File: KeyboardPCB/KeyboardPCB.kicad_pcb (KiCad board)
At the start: 2 copper layers, 182 parts, among them P1 USB_C_Plug, P2 USB_C_Plug, Q1 CSD17527Q5A, Q2 CSD17527Q5A, U1 ATmega32U4-M, U2 TPS61236PRWLT, U3 BQ297xy, U4 BQ24193RGER, Y1 ECS-160-7-33B-CKL-TR

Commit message: Began work on PCB
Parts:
- moved D7 160.3 mm to (25.4, 157.5), turned to 90 degrees
- moved Y1 156.5 mm to (36.7, 34.0)
- moved D6 147.1 mm to (25.4, 134.6), turned to 90 degrees
- moved D12 144.0 mm to (36.3, 157.5), turned to 90 degrees
- moved D5 135.8 mm to (25.4, 111.8), turned to 90 degrees
- moved D16 135.3 mm to (50.5, 136.5), turned to 90 degrees
- moved R3 132.4 mm to (35.6, 27.9)
- moved D11 127.8 mm to (38.1, 131.4), turned to 90 degrees
- moved D4 127.6 mm to (25.4, 90.7), turned to 90 degrees
- moved C2 124.8 mm to (44.0, 35.6)
- moved C1 124.7 mm to (44.0, 33.0)
- moved D3 121.9 mm to (25.4, 71.1), turned to 90 degrees
- moved D15 120.2 mm to (53.0, 114.3), turned to 90 degrees
- moved C9 119.3 mm to (55.9, 22.9), turned to -90 degrees
- moved D20 119.2 mm to (63.5, 136.5), turned to 90 degrees
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
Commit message: Changed switch and revised PCB layout?
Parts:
- BT1, C1, C11, C2, C3, C4, C5, C6, C7, C8, C9, L1, L2, LED1, LED2, LED3, LED4, LED5, P1, P2, Q1, Q2, R1, R10, R11, R12, R13, R14, R15, R16, R2, R3, R4, R5, R6, R7, R8, R9, S1, U1, U2, U3, U4, Y1: moved to B.Cu
- S10, S11, S12, S13, S14, S15, S16, S17, S18, S19, S2, S20, S21, S22, S23, S24, S25, S26, S27, S28, S29, S3, S30, S31, S32, S33, S34, S35, S36, S37, S38, S39, S4, S40, S41, S42, S43, S44, S45, S46, S47, S48, S49, S5, S50, S51, S52, S53, S54, S55, S56, S57, S58, S59, S6, S60, S61, S62, S63, S64, S65, S66, S67, S68, S69, S7, S70, S8, S9: footprint keyboard_syms:B3FS1012P -> keyboard_syms:B3U1100PB
- moved D7 249.8 mm to (245.0, 38.4), turned to 0 degrees
- moved D6 240.7 mm to (245.0, 36.0), turned to 0 degrees
- moved D12 234.4 mm to (245.0, 50.7), turned to 0 degrees
- moved D5 233.1 mm to (245.0, 33.5), turned to 0 degrees
- moved D4 227.5 mm to (245.0, 31.1), turned to 0 degrees
- moved D16 224.3 mm to (248.6, 31.1), turned to 0 degrees
- moved D3 223.6 mm to (245.0, 28.6), turned to 0 degrees
- moved D11 223.0 mm to (245.0, 48.2), turned to 0 degrees
- moved D10 216.7 mm to (245.0, 45.8), turned to 0 degrees
- moved D15 213.5 mm to (248.6, 28.6), turned to 0 degrees
- moved D9 212.7 mm to (245.0, 43.3), turned to 0 degrees
- moved D8 211.9 mm to (245.0, 40.9), turned to 0 degrees
- moved D20 208.3 mm to (248.6, 40.9), turned to 0 degrees
- moved U1 201.6 mm to (207.3, 122.4), turned to 180 degrees
- moved D19 199.7 mm to (248.6, 38.4), turned to 0 degrees
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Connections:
- D22 pad 2: Net-(D22-A) -> unconnected-(D22-A-Pad2)
- D25 pad 2: Net-(D25-A) -> unconnected-(D25-A-Pad2)
- D29 pad 2: Net-(D29-A) -> unconnected-(D29-A-Pad2)
- D38 pad 2: Net-(D38-A) -> unconnected-(D38-A-Pad2)
- D39 pad 2: Net-(D39-A) -> unconnected-(D39-A-Pad2)
- S10 pad 1: unconnected-(S10-C1-Pad1) -> /Key_Array/ICOL1
- S10 pad 2: /Key_Array/ICOL1 -> Net-(D11-A)
- S10 pad 3: Net-(D11-A) -> unconnected-(S10-NC-Pad3)
- S11 pad 1: unconnected-(S11-C1-Pad1) -> /Key_Array/ICOL1
- S11 pad 2: /Key_Array/ICOL1 -> Net-(D12-A)
- S11 pad 3: Net-(D12-A) -> unconnected-(S11-NC-Pad3)
- S12 pad 1: unconnected-(S12-C1-Pad1) -> /Key_Array/ICOL2
- S12 pad 2: /Key_Array/ICOL2 -> Net-(D13-A)
- S12 pad 3: Net-(D13-A) -> unconnected-(S12-NC-Pad3)
- S13 pad 1: unconnected-(S13-C1-Pad1) -> /Key_Array/ICOL2
- S13 pad 2: /Key_Array/ICOL2 -> Net-(D14-A)
- S13 pad 3: Net-(D14-A) -> unconnected-(S13-NC-Pad3)
- S14 pad 1: unconnected-(S14-C1-Pad1) -> /Key_Array/ICOL2
- S14 pad 2: /Key_Array/ICOL2 -> Net-(D15-A)
- S14 pad 3: Net-(D15-A) -> unconnected-(S14-NC-Pad3)
- S15 pad 1: unconnected-(S15-C1-Pad1) -> /Key_Array/ICOL2
- S15 pad 2: /Key_Array/ICOL2 -> Net-(D16-A)
- S15 pad 3: Net-(D16-A) -> unconnected-(S15-NC-Pad3)
- S16 pad 1: unconnected-(S16-C1-Pad1) -> /Key_Array/ICOL3
- S16 pad 2: /Key_Array/ICOL3 -> Net-(D17-A)
- S16 pad 3: Net-(D17-A) -> unconnected-(S16-NC-Pad3)
- S17 pad 1: unconnected-(S17-C1-Pad1) -> /Key_Array/ICOL3
- S17 pad 2: /Key_Array/ICOL3 -> Net-(D18-A)
- S17 pad 3: Net-(D18-A) -> unconnected-(S17-NC-Pad3)
- S18 pad 1: unconnected-(S18-C1-Pad1) -> /Key_Array/ICOL3
- S18 pad 2: /Key_Array/ICOL3 -> Net-(D19-A)
- S18 pad 3: Net-(D19-A) -> unconnected-(S18-NC-Pad3)
- S19 pad 1: unconnected-(S19-C1-Pad1) -> /Key_Array/ICOL3
- S19 pad 2: /Key_Array/ICOL3 -> Net-(D20-A)
- S19 pad 3: Net-(D20-A) -> unconnected-(S19-NC-Pad3)
- S2 pad 1: unconnected-(S2-C1-Pad1) -> /Key_Array/ICOL0
- S2 pad 2: /Key_Array/ICOL0 -> Net-(D3-A)
- S2 pad 3: Net-(D3-A) -> unconnected-(S2-NC-Pad3)
- S20 pad 1: unconnected-(S20-C1-Pad1) -> /Key_Array/ICOL4
- S20 pad 2: /Key_Array/ICOL4 -> Net-(D21-A)
- S20 pad 3: Net-(D21-A) -> unconnected-(S20-NC-Pad3)
- S21 pad 1: unconnected-(S21-C1-Pad1) -> /Key_Array/ICOL4
- S21 pad 2: /Key_Array/ICOL4 -> unconnected-(S21-C2-Pad2)
- S21 pad 3: Net-(D22-A) -> unconnected-(S21-NC-Pad3)
- S22 pad 1: unconnected-(S22-C1-Pad1) -> /Key_Array/ICOL4
- S22 pad 2: /Key_Array/ICOL4 -> Net-(D23-A)
- S22 pad 3: Net-(D23-A) -> unconnected-(S22-NC-Pad3)
- S23 pad 1: unconnected-(S23-C1-Pad1) -> /Key_Array/ICOL4
- S23 pad 2: /Key_Array/ICOL4 -> Net-(D24-A)
- S23 pad 3: Net-(D24-A) -> unconnected-(S23-NC-Pad3)
- S24 pad 2: /Key_Array/ICOL5 -> unconnected-(S24-C2-Pad2)
- S24 pad 3: Net-(D25-A) -> unconnected-(S24-NC-Pad3)
- S25 pad 1: unconnected-(S25-C1-Pad1) -> /Key_Array/ICOL5
- S25 pad 2: /Key_Array/ICOL5 -> Net-(D26-A)
- S25 pad 3: Net-(D26-A) -> unconnected-(S25-NC-Pad3)
- S26 pad 1: unconnected-(S26-C1-Pad1) -> /Key_Array/ICOL5
- S26 pad 2: /Key_Array/ICOL5 -> Net-(D27-A)
- S26 pad 3: Net-(D27-A) -> unconnected-(S26-NC-Pad3)
- S27 pad 1: unconnected-(S27-C1-Pad1) -> /Key_Array/ICOL5
- S27 pad 2: /Key_Array/ICOL5 -> Net-(D28-A)
- S27 pad 3: Net-(D28-A) -> unconnected-(S27-NC-Pad3)
- S28 pad 2: /Key_Array/ICOL6 -> unconnected-(S28-C2-Pad2)
- S28 pad 3: Net-(D29-A) -> unconnected-(S28-NC-Pad3)
- S29 pad 1: unconnected-(S29-C1-Pad1) -> /Key_Array/ICOL6
- S29 pad 2: /Key_Array/ICOL6 -> Net-(D30-A)
- S29 pad 3: Net-(D30-A) -> unconnected-(S29-NC-Pad3)
- S3 pad 1: unconnected-(S3-C1-Pad1) -> /Key_Array/ICOL0
- S3 pad 2: /Key_Array/ICOL0 -> Net-(D4-A)
- S3 pad 3: Net-(D4-A) -> unconnected-(S3-NC-Pad3)
- S30 pad 1: unconnected-(S30-C1-Pad1) -> /Key_Array/ICOL6
- S30 pad 2: /Key_Array/ICOL6 -> Net-(D31-A)
- S30 pad 3: Net-(D31-A) -> unconnected-(S30-NC-Pad3)
- S31 pad 1: unconnected-(S31-C1-Pad1) -> /Key_Array/ICOL6
- S31 pad 2: /Key_Array/ICOL6 -> Net-(D32-A)
- S31 pad 3: Net-(D32-A) -> unconnected-(S31-NC-Pad3)
- S32 pad 1: unconnected-(S32-C1-Pad1) -> /Key_Array/ICOL6
- S32 pad 2: /Key_Array/ICOL6 -> Net-(D33-A)
- S32 pad 3: Net-(D33-A) -> unconnected-(S32-NC-Pad3)
- S33 pad 1: unconnected-(S33-C1-Pad1) -> /Key_Array/ICOL7
- S33 pad 2: /Key_Array/ICOL7 -> Net-(D34-A)
- S33 pad 3: Net-(D34-A) -> unconnected-(S33-NC-Pad3)
- S34 pad 1: unconnected-(S34-C1-Pad1) -> /Key_Array/ICOL7
- S34 pad 2: /Key_Array/ICOL7 -> Net-(D35-A)
- S34 pad 3: Net-(D35-A) -> unconnected-(S34-NC-Pad3)
- S35 pad 1: unconnected-(S35-C1-Pad1) -> /Key_Array/ICOL7
- S35 pad 2: /Key_Array/ICOL7 -> Net-(D36-A)
- S35 pad 3: Net-(D36-A) -> unconnected-(S35-NC-Pad3)
- S36 pad 1: unconnected-(S36-C1-Pad1) -> /Key_Array/ICOL7
- S36 pad 2: /Key_Array/ICOL7 -> Net-(D37-A)
- S36 pad 3: Net-(D37-A) -> unconnected-(S36-NC-Pad3)
- S37 pad 1: unconnected-(S37-C1-Pad1) -> /Key_Array/ICOL7
- S37 pad 2: /Key_Array/ICOL7 -> unconnected-(S37-C2-Pad2)
- S37 pad 3: Net-(D38-A) -> unconnected-(S37-NC-Pad3)
- S38 pad 2: /Key_Array/ICOL8 -> unconnected-(S38-C2-Pad2)
- S38 pad 3: Net-(D39-A) -> unconnected-(S38-NC-Pad3)
- S39 pad 1: unconnected-(S39-C1-Pad1) -> /Key_Array/ICOL8
- S39 pad 2: /Key_Array/ICOL8 -> Net-(D40-A)
- S39 pad 3: Net-(D40-A) -> unconnected-(S39-NC-Pad3)
- S4 pad 1: unconnected-(S4-C1-Pad1) -> /Key_Array/ICOL0
- S4 pad 2: /Key_Array/ICOL0 -> Net-(D5-A)
- S4 pad 3: Net-(D5-A) -> unconnected-(S4-NC-Pad3)
- S40 pad 1: unconnected-(S40-C1-Pad1) -> /Key_Array/ICOL8
- S40 pad 2: /Key_Array/ICOL8 -> Net-(D41-A)
- S40 pad 3: Net-(D41-A) -> unconnected-(S40-NC-Pad3)
- S41 pad 1: unconnected-(S41-C1-Pad1) -> /Key_Array/ICOL8
- S41 pad 2: /Key_Array/ICOL8 -> Net-(D42-A)
- S41 pad 3: Net-(D42-A) -> unconnected-(S41-NC-Pad3)
- S42 pad 1: unconnected-(S42-C1-Pad1) -> /Key_Array/ICOL9
- S42 pad 2: /Key_Array/ICOL9 -> Net-(D43-A)
- S42 pad 3: Net-(D43-A) -> unconnected-(S42-NC-Pad3)
- S43 pad 1: unconnected-(S43-C1-Pad1) -> /Key_Array/ICOL9
- S43 pad 2: /Key_Array/ICOL9 -> Net-(D44-A)
- S43 pad 3: Net-(D44-A) -> unconnected-(S43-NC-Pad3)
- S44 pad 1: unconnected-(S44-C1-Pad1) -> /Key_Array/ICOL9
- S44 pad 2: /Key_Array/ICOL9 -> Net-(D45-A)
- S44 pad 3: Net-(D45-A) -> unconnected-(S44-NC-Pad3)
- S45 pad 1: unconnected-(S45-C1-Pad1) -> /Key_Array/ICOL9
- S45 pad 2: /Key_Array/ICOL9 -> Net-(D46-A)
- S45 pad 3: Net-(D46-A) -> unconnected-(S45-NC-Pad3)
- S46 pad 1: unconnected-(S46-C1-Pad1) -> /Key_Array/ICOL10
- S46 pad 2: /Key_Array/ICOL10 -> Net-(D47-A)
- S46 pad 3: Net-(D47-A) -> unconnected-(S46-NC-Pad3)
- S47 pad 1: unconnected-(S47-C1-Pad1) -> /Key_Array/ICOL10
- S47 pad 2: /Key_Array/ICOL10 -> Net-(D48-A)
- S47 pad 3: Net-(D48-A) -> unconnected-(S47-NC-Pad3)
- S48 pad 1: unconnected-(S48-C1-Pad1) -> /Key_Array/ICOL10
- S48 pad 2: /Key_Array/ICOL10 -> Net-(D49-A)
- S48 pad 3: Net-(D49-A) -> unconnected-(S48-NC-Pad3)
- S49 pad 1: unconnected-(S49-C1-Pad1) -> /Key_Array/ICOL10
- S49 pad 2: /Key_Array/ICOL10 -> Net-(D50-A)
- S49 pad 3: Net-(D50-A) -> unconnected-(S49-NC-Pad3)
- S5 pad 1: unconnected-(S5-C1-Pad1) -> /Key_Array/ICOL0
- S5 pad 2: /Key_Array/ICOL0 -> Net-(D6-A)
- S5 pad 3: Net-(D6-A) -> unconnected-(S5-NC-Pad3)
- S50 pad 1: unconnected-(S50-C1-Pad1) -> /Key_Array/ICOL11
- S50 pad 2: /Key_Array/ICOL11 -> Net-(D51-A)
- S50 pad 3: Net-(D51-A) -> unconnected-(S50-NC-Pad3)
- S51 pad 1: unconnected-(S51-C1-Pad1) -> /Key_Array/ICOL11
- S51 pad 2: /Key_Array/ICOL11 -> Net-(D52-A)
- S51 pad 3: Net-(D52-A) -> unconnected-(S51-NC-Pad3)
- S52 pad 1: unconnected-(S52-C1-Pad1) -> /Key_Array/ICOL11
- S52 pad 2: /Key_Array/ICOL11 -> Net-(D53-A)
- S52 pad 3: Net-(D53-A) -> unconnected-(S52-NC-Pad3)
- S53 pad 1: unconnected-(S53-C1-Pad1) -> /Key_Array/ICOL11
- S53 pad 2: /Key_Array/ICOL11 -> Net-(D54-A)
- S53 pad 3: Net-(D54-A) -> unconnected-(S53-NC-Pad3)
- S54 pad 1: unconnected-(S54-C1-Pad1) -> /Key_Array/ICOL11
- S54 pad 2: /Key_Array/ICOL11 -> Net-(D55-A)
- S54 pad 3: Net-(D55-A) -> unconnected-(S54-NC-Pad3)
- S55 pad 1: unconnected-(S55-C1-Pad1) -> /Key_Array/ICOL12
- S55 pad 2: /Key_Array/ICOL12 -> Net-(D56-A)
- S55 pad 3: Net-(D56-A) -> unconnected-(S55-NC-Pad3)
- S56 pad 1: unconnected-(S56-C1-Pad1) -> /Key_Array/ICOL12
- S56 pad 2: /Key_Array/ICOL12 -> Net-(D57-A)
- S56 pad 3: Net-(D57-A) -> unconnected-(S56-NC-Pad3)
- S57 pad 1: unconnected-(S57-C1-Pad1) -> /Key_Array/ICOL12
- S57 pad 2: /Key_Array/ICOL12 -> Net-(D58-A)
- S57 pad 3: Net-(D58-A) -> unconnected-(S57-NC-Pad3)
- S58 pad 1: unconnected-(S58-C1-Pad1) -> /Key_Array/ICOL12
- S58 pad 2: /Key_Array/ICOL12 -> Net-(D59-A)
- S58 pad 3: Net-(D59-A) -> unconnected-(S58-NC-Pad3)
- S59 pad 1: unconnected-(S59-C1-Pad1) -> /Key_Array/ICOL12
- S59 pad 2: /Key_Array/ICOL12 -> Net-(D60-A)
- S59 pad 3: Net-(D60-A) -> unconnected-(S59-NC-Pad3)
- S6 pad 1: unconnected-(S6-C1-Pad1) -> /Key_Array/ICOL0
- S6 pad 2: /Key_Array/ICOL0 -> Net-(D7-A)
- S6 pad 3: Net-(D7-A) -> unconnected-(S6-NC-Pad3)
- S60 pad 1: unconnected-(S60-C1-Pad1) -> /Key_Array/ICOL13
- S60 pad 2: /Key_Array/ICOL13 -> Net-(D61-A)
- S60 pad 3: Net-(D61-A) -> unconnected-(S60-NC-Pad3)
- S61 pad 1: unconnected-(S61-C1-Pad1) -> /Key_Array/ICOL13
- S61 pad 2: /Key_Array/ICOL13 -> Net-(D62-A)
- S61 pad 3: Net-(D62-A) -> unconnected-(S61-NC-Pad3)
- S62 pad 1: unconnected-(S62-C1-Pad1) -> /Key_Array/ICOL13
- S62 pad 2: /Key_Array/ICOL13 -> Net-(D63-A)
- S62 pad 3: Net-(D63-A) -> unconnected-(S62-NC-Pad3)
- S63 pad 1: unconnected-(S63-C1-Pad1) -> /Key_Array/ICOL13
- S63 pad 2: /Key_Array/ICOL13 -> Net-(D64-A)
- S63 pad 3: Net-(D64-A) -> unconnected-(S63-NC-Pad3)
- S64 pad 1: unconnected-(S64-C1-Pad1) -> /Key_Array/ICOL13
- S64 pad 2: /Key_Array/ICOL13 -> Net-(D65-A)
- S64 pad 3: Net-(D65-A) -> unconnected-(S64-NC-Pad3)
- S65 pad 1: unconnected-(S65-C1-Pad1) -> /Key_Array/ICOL14
- S65 pad 2: /Key_Array/ICOL14 -> Net-(D66-A)
- S65 pad 3: Net-(D66-A) -> unconnected-(S65-NC-Pad3)
- S66 pad 1: unconnected-(S66-C1-Pad1) -> /Key_Array/ICOL14
- S66 pad 2: /Key_Array/ICOL14 -> Net-(D67-A)
- S66 pad 3: Net-(D67-A) -> unconnected-(S66-NC-Pad3)
- S67 pad 1: unconnected-(S67-C1-Pad1) -> /Key_Array/ICOL14
- S67 pad 2: /Key_Array/ICOL14 -> Net-(D68-A)
- S67 pad 3: Net-(D68-A) -> unconnected-(S67-NC-Pad3)
- S68 pad 1: unconnected-(S68-C1-Pad1) -> /Key_Array/ICOL15
- S68 pad 2: /Key_Array/ICOL15 -> Net-(D69-A)
- S68 pad 3: Net-(D69-A) -> unconnected-(S68-NC-Pad3)
- S69 pad 1: unconnected-(S69-C1-Pad1) -> /Key_Array/ICOL15
- S69 pad 2: /Key_Array/ICOL15 -> Net-(D70-A)
- S69 pad 3: Net-(D70-A) -> unconnected-(S69-NC-Pad3)
- S7 pad 1: unconnected-(S7-C1-Pad1) -> /Key_Array/ICOL1
- S7 pad 2: /Key_Array/ICOL1 -> Net-(D8-A)
- S7 pad 3: Net-(D8-A) -> unconnected-(S7-NC-Pad3)
- S70 pad 1: unconnected-(S70-C1-Pad1) -> /Key_Array/ICOL15
- S70 pad 2: /Key_Array/ICOL15 -> Net-(D71-A)
- S70 pad 3: Net-(D71-A) -> unconnected-(S70-NC-Pad3)
- S8 pad 1: unconnected-(S8-C1-Pad1) -> /Key_Array/ICOL1
- S8 pad 2: /Key_Array/ICOL1 -> Net-(D9-A)
- S8 pad 3: Net-(D9-A) -> unconnected-(S8-NC-Pad3)
- S9 pad 1: unconnected-(S9-C1-Pad1) -> /Key_Array/ICOL1
- S9 pad 2: /Key_Array/ICOL1 -> Net-(D10-A)
- S9 pad 3: Net-(D10-A) -> unconnected-(S9-NC-Pad3)
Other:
- board outline added: 81.3 x 50.8 mm
- board text added: "1"
- board text added: "Esc"
- board text added: "Q1"

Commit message: Finalised schematic, progress on board layout
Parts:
- removed C11: UMK107ABJ105KA8T, keyboard_syms:CAPC1608X95N
- removed D68, D69, D70, D71: 1N4148WT, Diode_SMD:D_SOD-523
- removed S69: MX_PGDN1, keyboard_syms:B3U1100PB
- removed S70: MX_FN1, keyboard_syms:B3U1100PB
- added C10: UMK107ABJ105KA8T, keyboard_syms:CAPC1608X95N, B.Cu at (210.9, 126.2)
- added D1: 1N4148WT, Diode_SMD:D_SOD-523, F.Cu at (63.5, 47.0)
- added D2: 1N4148WT, Diode_SMD:D_SOD-523, F.Cu at (63.5, 58.4)
- C1: value GRM21BC81C226ME44L -> UMK107ABJ105KA8T; footprint keyboard_syms:CAPC2012X145N -> keyboard_syms:CAPC1608X95N
- C3, C5: value UMK107ABJ105KA8T -> GRM21BC81C226ME44L; footprint keyboard_syms:CAPC1608X95N -> keyboard_syms:CAPC2012X145N
- C4: value C0603C104K1RACAUTO -> UMK107ABJ105KA8T
- C6: value MSASJ021SB5472KWNA01 -> GRM21BC81C226ME44L; footprint keyboard_syms:CAPC0201X14N -> keyboard_syms:CAPC2012X145N
- C8: value GRM21BC81C226ME44L -> MSASJ021SB5472KWNA01; footprint keyboard_syms:CAPC2012X145N -> keyboard_syms:CAPC0201X14N
- C9: value GRM21BC81C226ME44L -> C0603C104K1RACAUTO; footprint keyboard_syms:CAPC2012X145N -> keyboard_syms:CAPC1608X95N
- R10: value CRMA1206AF10K0DKEF -> RG3216P-5004-B-T1; footprint keyboard_syms:RESC3216X74N -> keyboard_syms:RESC3216X50N
- R12: value RP0603BRD072K2L -> RG3216P-5004-B-T1; footprint keyboard_syms:RESC1608X55N -> keyboard_syms:RESC3216X50N
- R13: value CRMA1206AF10K0DKEF -> ERJ-H2RD2200X; footprint keyboard_syms:RESC3216X74N -> keyboard_syms:H2C_H2R
- R15: value RG3216P-5004-B-T1 -> CRMA1206AF10K0DKEF; footprint keyboard_syms:RESC3216X50N -> keyboard_syms:RESC3216X74N
- R16: value RG3216P-5004-B-T1 -> ERA-8KEB3303V; footprint keyboard_syms:RESC3216X50N -> keyboard_syms:ERA8KEB1004V
- R4: value ERA-8KEB3303V -> CRMA1206AF10K0DKEF; footprint keyboard_syms:ERA8KEB1004V -> keyboard_syms:RESC3216X74N
- R6: value ERJ-H2RD2200X -> RP0603BRD072K2L; footprint keyboard_syms:H2C_H2R -> keyboard_syms:RESC1608X55N
- S16: value MX_NM3 -> MX_FN1
- S17: value MX_E1 -> MX_NM3
- S18: value MX_D1 -> MX_E1
- S19: value MX_X1 -> MX_D1
- S20: value MX_NM4 -> MX_X1
- S21: value MX_R1 -> MX_FN2
- S22: value MX_F1 -> MX_NM4
- S23: value MX_C1 -> MX_R1
- S24: value MX_NM5 -> MX_F1
- S25: value MX_T1 -> MX_C1
- S26: value MX_G1 -> MX_PGUP1
- S27: value MX_V1 -> MX_NM5
- S28: value MX_NM6 -> MX_T1
- S29: value MX_Y1 -> MX_G1
- S30: value MX_H1 -> MX_V1
- S31: value MX_B1 -> MX_PGDN1
- S32: value MX_LSPCE1 -> MX_NM6
- S33: value MX_NM7 -> MX_Y1
- S34: value MX_U1 -> MX_H1
- S35: value MX_J1 -> MX_B1
- S36: value MX_N1 -> MX_LSPCE1
- S37: value MX_RSPCE1 -> MX_NM7
- S38: value MX_NM8 -> MX_U1
- S39: value MX_I1 -> MX_J1
- S40: value MX_J1 -> MX_N1
- S41: value MX_M1 -> MX_RSPCE1
- S42: value MX_NM9 -> MX_NM8
- S43: value MX_O1 -> MX_I1
- S45: value MX_,1 -> MX_M1
- S46: value MX_NM0 -> MX_LEFT1
- S47: value MX_P1 -> MX_NM9
- S48: value MX_L1 -> MX_O1
- S49: value MX_.1 -> MX_L1
- S50: value MX_-1 -> MX_,1
- S51: value MX_[1 -> MX_DOWN1
- S52: value MX_;1 -> MX_NM0
- S53: value MX_/1 -> MX_P1
- S54: value MX_RALT1 -> MX_;1
- S55: value MX_=1 -> MX_.1
- S56: value MX_]1 -> MX_UP1
- S57: value MX_'1 -> MX_-1
- S58: value MX_RSHIFT1 -> MX_[1
- S59: value MX_LEFT1 -> MX_'1
- S60: value MX_BKSPC1 -> MX_/1
- S61: value MX_\1 -> MX_RIGHT1
- S62: value MX_ENTER1 -> MX_=1
- S63: value MX_UP1 -> MX_]1
- S64: value MX_DOWN1 -> MX_RSUP1
- S65: value MX_DEL1 -> MX_\1
- S66: value MX_FN2 -> MX_ENTER1
- S67: value MX_RIGHT1 -> MX_BKSPC1
- S68: value MX_PGUP1 -> MX_DEL1
- U3: value BQ297xy -> BQ24193RGER; footprint Package_SON:WSON-6_1.5x1.5mm_P0.5mm -> keyboard_syms:QFN50P400X400X100-25N-D
- U4: value BQ24193RGER -> BQ297xy; footprint keyboard_syms:QFN50P400X400X100-25N-D -> Package_SON:WSON-6_1.5x1.5mm_P0.5mm
- moved D5 189.7 mm to (63.5, 88.7), turned to 90 degrees
- moved D4 187.6 mm to (63.5, 78.7), turned to 90 degrees
- moved D3 185.8 mm to (63.5, 68.6), turned to 90 degrees
- moved D15 184.9 mm to (73.7, 88.7), turned to 90 degrees
- moved D10 181.6 mm to (68.6, 88.9), turned to 90 degrees
- moved D9 179.9 mm to (68.6, 78.7), turned to 90 degrees
- moved D7 177.4 mm to (68.6, 57.1), turned to 90 degrees
- moved D8 177.3 mm to (69.8, 68.6), turned to 90 degrees
- moved D6 176.7 mm to (68.6, 47.0), turned to 90 degrees
- moved D20 174.1 mm to (81.3, 89.2), turned to 90 degrees
- moved D19 170.8 mm to (82.5, 78.7), turned to 90 degrees
- moved D14 170.3 mm to (76.2, 78.0), turned to 90 degrees
- moved D13 169.4 mm to (76.2, 67.9), turned to 90 degrees
- moved D18 169.1 mm to (82.5, 67.9), turned to 90 degrees
- moved D17 169.0 mm to (81.3, 57.2), turned to 90 degrees
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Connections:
- C1 pad 2: Net-(U1-XTAL1) -> +5V
- C2 pad 2: Net-(U1-XTAL2) -> Net-(U1-XTAL1)
- C3 pad 2: Net-(U1-UCAP) -> Net-(U1-XTAL2)
- C4 pad 1: -BATT -> GND
- C4 pad 2: Net-(U3-BAT) -> Net-(U1-UCAP)
- C5 pad 1: GND -> /MCU_Battery/VBUSOUT
- C5 pad 2: +5V -> GND
- C6 pad 1: Net-(U4-SW_1) -> /MCU_Battery/VBUSOUT
- C6 pad 2: Net-(U4-BTST) -> GND
- C8 pad 1: /MCU_Battery/VBUSOUT -> Net-(U3-SW_1)
- C8 pad 2: GND -> Net-(U3-BTST)
- C9 pad 1: /MCU_Battery/VBUSOUT -> -BATT
- C9 pad 2: GND -> Net-(U4-BAT)
- D10 pad 1: /Key_Array/IROW2 -> /Key_Array/IROW4
- D11 pad 1: /Key_Array/IROW3 -> /Key_Array/IROW0
- D12 pad 1: /Key_Array/IROW4 -> /Key_Array/IROW1
- D13 pad 1: /Key_Array/IROW0 -> /Key_Array/IROW2
- D14 pad 1: /Key_Array/IROW1 -> /Key_Array/IROW3
- D15 pad 1: /Key_Array/IROW2 -> /Key_Array/IROW4
- D16 pad 1: /Key_Array/IROW3 -> /Key_Array/IROW0
- D17 pad 1: /Key_Array/IROW0 -> /Key_Array/IROW1
- D18 pad 1: /Key_Array/IROW1 -> /Key_Array/IROW2
- D19 pad 1: /Key_Array/IROW2 -> /Key_Array/IROW3
- D20 pad 1: /Key_Array/IROW3 -> /Key_Array/IROW4
- D22 pad 2: unconnected-(D22-A-Pad2) -> Net-(D22-A)
- D25 pad 1: /Key_Array/IROW0 -> /Key_Array/IROW4
- D25 pad 2: unconnected-(D25-A-Pad2) -> Net-(D25-A)
- D26 pad 1: /Key_Array/IROW1 -> /Key_Array/IROW0
- D27 pad 1: /Key_Array/IROW2 -> /Key_Array/IROW1
- D28 pad 1: /Key_Array/IROW3 -> /Key_Array/IROW2
- D29 pad 1: /Key_Array/IROW0 -> /Key_Array/IROW3
- D29 pad 2: unconnected-(D29-A-Pad2) -> Net-(D29-A)
- D3 pad 1: /Key_Array/IROW0 -> /Key_Array/IROW2
- D30 pad 1: /Key_Array/IROW1 -> /Key_Array/IROW4
- D31 pad 1: /Key_Array/IROW2 -> /Key_Array/IROW0
- D32 pad 1: /Key_Array/IROW3 -> /Key_Array/IROW1
- D33 pad 1: /Key_Array/IROW4 -> /Key_Array/IROW2
- D34 pad 1: /Key_Array/IROW0 -> /Key_Array/IROW3
- D35 pad 1: /Key_Array/IROW1 -> /Key_Array/IROW4
- D36 pad 1: /Key_Array/IROW2 -> /Key_Array/IROW0
- D37 pad 1: /Key_Array/IROW3 -> /Key_Array/IROW1
- D38 pad 1: /Key_Array/IROW4 -> /Key_Array/IROW2
- D38 pad 2: unconnected-(D38-A-Pad2) -> Net-(D38-A)
- D39 pad 1: /Key_Array/IROW0 -> /Key_Array/IROW3
- D39 pad 2: unconnected-(D39-A-Pad2) -> Net-(D39-A)
- D4 pad 1: /Key_Array/IROW1 -> /Key_Array/IROW3
- D40 pad 1: /Key_Array/IROW1 -> /Key_Array/IROW4
- D41 pad 1: /Key_Array/IROW2 -> /Key_Array/IROW0
- D42 pad 1: /Key_Array/IROW3 -> /Key_Array/IROW1
- D43 pad 1: /Key_Array/IROW0 -> /Key_Array/IROW2
- D44 pad 1: /Key_Array/IROW1 -> /Key_Array/IROW3
- D45 pad 1: /Key_Array/IROW2 -> /Key_Array/IROW4
- D46 pad 1: /Key_Array/IROW3 -> /Key_Array/IROW0
- D47 pad 1: /Key_Array/IROW0 -> /Key_Array/IROW1
- D48 pad 1: /Key_Array/IROW1 -> /Key_Array/IROW2
- D49 pad 1: /Key_Array/IROW2 -> /Key_Array/IROW3
- D5 pad 1: /Key_Array/IROW2 -> /Key_Array/IROW4
- D50 pad 1: /Key_Array/IROW3 -> /Key_Array/IROW4
- D6 pad 1: /Key_Array/IROW3 -> /Key_Array/IROW0
- D67 pad 1: /Key_Array/IROW3 -> /Key_Array/IROW1
- D7 pad 1: /Key_Array/IROW4 -> /Key_Array/IROW1
- D8 pad 1: /Key_Array/IROW0 -> /Key_Array/IROW2
- D9 pad 1: /Key_Array/IROW1 -> /Key_Array/IROW3
- L2 pad 1: Net-(U4-SYS_1) -> Net-(U3-SYS_1)
- L2 pad 2: Net-(U4-BTST) -> Net-(U3-BTST)
- LED1 pad 1: Net-(LED1-K) -> GND
- LED2 pad 1: GND -> Net-(LED2-K)
- LED5 pad 1: Net-(LED2-A) -> Net-(LED1-A)
- R10 pad 1: GND -> Net-(Q1-G)
- R10 pad 2: +BATT -> GND
- R11 pad 1: Net-(U4-ILIM) -> Net-(LED1-A)
- R11 pad 2: GND -> Net-(U3-STAT)
- R12 pad 1: GND -> Net-(Q2-G)
- R12 pad 2: Net-(U3-V-) -> Net-(Q1-D)
- R13 pad 1: Net-(U4-TS1) -> Net-(U3-ILIM)
- R13 pad 2: Net-(U4-REGN) -> GND
- R14 pad 1: GND -> Net-(U3-TS1)
- R14 pad 2: Net-(U4-TS1) -> Net-(U3-REGN)
- R15 pad 1: Net-(Q1-G) -> GND
- R15 pad 2: GND -> Net-(U3-TS1)
- R16 pad 1: Net-(Q2-G) -> Net-(U4-BAT)
- R16 pad 2: Net-(Q1-D) -> +BATT
- R4 pad 1: Net-(U3-BAT) -> Net-(U1-~{HWB}/PE2)
- R4 pad 2: +BATT -> GND
- R5 pad 1: Net-(U1-~{HWB}/PE2) -> GND
- R5 pad 2: GND -> +BATT
- R6 pad 1: Net-(LED1-K) -> GND
- R6 pad 2: GND -> Net-(U4-V-)
- R7 pad 1: Net-(LED4-K) -> Net-(LED2-K)
- R9 pad 1: Net-(LED2-A) -> Net-(LED4-K)
- R9 pad 2: Net-(U4-STAT) -> GND
- S10 pad 2: Net-(D11-A) -> Net-(D9-A)
- S11 pad 2: Net-(D12-A) -> Net-(D10-A)
- S12 pad 2: Net-(D13-A) -> Net-(D11-A)
- S13 pad 2: Net-(D14-A) -> Net-(D12-A)
- S14 pad 2: Net-(D15-A) -> Net-(D13-A)
- S15 pad 2: Net-(D16-A) -> Net-(D14-A)
- S16 pad 1: /Key_Array/ICOL3 -> /Key_Array/ICOL2
- S16 pad 2: Net-(D17-A) -> Net-(D15-A)
- S17 pad 2: Net-(D18-A) -> Net-(D16-A)
- S18 pad 2: Net-(D19-A) -> Net-(D17-A)
- S19 pad 2: Net-(D20-A) -> Net-(D18-A)
- S2 pad 2: Net-(D3-A) -> Net-(D1-A)
- S20 pad 1: /Key_Array/ICOL4 -> /Key_Array/ICOL3
- S20 pad 2: Net-(D21-A) -> Net-(D19-A)
- S21 pad 1: /Key_Array/ICOL4 -> /Key_Array/ICOL3
- S21 pad 2: unconnected-(S21-C2-Pad2) -> Net-(D20-A)
- S22 pad 2: Net-(D23-A) -> Net-(D21-A)
- S23 pad 2: Net-(D24-A) -> Net-(D22-A)
- S24 pad 1: unconnected-(S24-C1-Pad1) -> /Key_Array/ICOL4
- S24 pad 2: unconnected-(S24-C2-Pad2) -> Net-(D23-A)
- S25 pad 1: /Key_Array/ICOL5 -> /Key_Array/ICOL4
- S25 pad 2: Net-(D26-A) -> Net-(D24-A)
- S26 pad 1: /Key_Array/ICOL5 -> /Key_Array/ICOL4
- S26 pad 2: Net-(D27-A) -> Net-(D25-A)
- S27 pad 2: Net-(D28-A) -> Net-(D26-A)
- S28 pad 1: unconnected-(S28-C1-Pad1) -> /Key_Array/ICOL5
- S28 pad 2: unconnected-(S28-C2-Pad2) -> Net-(D27-A)
- S29 pad 1: /Key_Array/ICOL6 -> /Key_Array/ICOL5
- S29 pad 2: Net-(D30-A) -> Net-(D28-A)
- S3 pad 2: Net-(D4-A) -> Net-(D2-A)
- S30 pad 1: /Key_Array/ICOL6 -> /Key_Array/ICOL5
- S30 pad 2: Net-(D31-A) -> Net-(D29-A)
- S31 pad 1: /Key_Array/ICOL6 -> /Key_Array/ICOL5
- S31 pad 2: Net-(D32-A) -> Net-(D30-A)
- S32 pad 2: Net-(D33-A) -> Net-(D31-A)
- S33 pad 1: /Key_Array/ICOL7 -> /Key_Array/ICOL6
- S33 pad 2: Net-(D34-A) -> Net-(D32-A)
- S34 pad 1: /Key_Array/ICOL7 -> /Key_Array/ICOL6
- S34 pad 2: Net-(D35-A) -> Net-(D33-A)
- S35 pad 1: /Key_Array/ICOL7 -> /Key_Array/ICOL6
- S35 pad 2: Net-(D36-A) -> Net-(D34-A)
- S36 pad 1: /Key_Array/ICOL7 -> /Key_Array/ICOL6
- S36 pad 2: Net-(D37-A) -> Net-(D35-A)
- S37 pad 2: unconnected-(S37-C2-Pad2) -> Net-(D36-A)
- S38 pad 1: unconnected-(S38-C1-Pad1) -> /Key_Array/ICOL7
- S38 pad 2: unconnected-(S38-C2-Pad2) -> Net-(D37-A)
- S39 pad 1: /Key_Array/ICOL8 -> /Key_Array/ICOL7
- S39 pad 2: Net-(D40-A) -> Net-(D38-A)
- S4 pad 2: Net-(D5-A) -> Net-(D3-A)
- S40 pad 1: /Key_Array/ICOL8 -> /Key_Array/ICOL7
- S40 pad 2: Net-(D41-A) -> Net-(D39-A)
- S41 pad 1: /Key_Array/ICOL8 -> /Key_Array/ICOL7
- S41 pad 2: Net-(D42-A) -> Net-(D40-A)
- S42 pad 1: /Key_Array/ICOL9 -> /Key_Array/ICOL8
- S42 pad 2: Net-(D43-A) -> Net-(D41-A)
- S43 pad 1: /Key_Array/ICOL9 -> /Key_Array/ICOL8
- S43 pad 2: Net-(D44-A) -> Net-(D42-A)
- S44 pad 1: /Key_Array/ICOL9 -> /Key_Array/ICOL8
- S44 pad 2: Net-(D45-A) -> Net-(D43-A)
- S45 pad 1: /Key_Array/ICOL9 -> /Key_Array/ICOL8
- S45 pad 2: Net-(D46-A) -> Net-(D44-A)
- S46 pad 1: /Key_Array/ICOL10 -> /Key_Array/ICOL8
- S46 pad 2: Net-(D47-A) -> Net-(D45-A)
- S47 pad 1: /Key_Array/ICOL10 -> /Key_Array/ICOL9
- S47 pad 2: Net-(D48-A) -> Net-(D46-A)
- S48 pad 1: /Key_Array/ICOL10 -> /Key_Array/ICOL9
- S48 pad 2: Net-(D49-A) -> Net-(D47-A)
- S49 pad 1: /Key_Array/ICOL10 -> /Key_Array/ICOL9
- S49 pad 2: Net-(D50-A) -> Net-(D48-A)
- S5 pad 2: Net-(D6-A) -> Net-(D4-A)
- S50 pad 1: /Key_Array/ICOL11 -> /Key_Array/ICOL9
- S50 pad 2: Net-(D51-A) -> Net-(D49-A)
- S51 pad 1: /Key_Array/ICOL11 -> /Key_Array/ICOL9
- S51 pad 2: Net-(D52-A) -> Net-(D50-A)
- S52 pad 1: /Key_Array/ICOL11 -> /Key_Array/ICOL10
- S52 pad 2: Net-(D53-A) -> Net-(D51-A)
- S53 pad 1: /Key_Array/ICOL11 -> /Key_Array/ICOL10
- S53 pad 2: Net-(D54-A) -> Net-(D52-A)
- S54 pad 1: /Key_Array/ICOL11 -> /Key_Array/ICOL10
- S54 pad 2: Net-(D55-A) -> Net-(D53-A)
- S55 pad 1: /Key_Array/ICOL12 -> /Key_Array/ICOL10
- S55 pad 2: Net-(D56-A) -> Net-(D54-A)
- S56 pad 1: /Key_Array/ICOL12 -> /Key_Array/ICOL10
- S56 pad 2: Net-(D57-A) -> Net-(D55-A)
- S57 pad 1: /Key_Array/ICOL12 -> /Key_Array/ICOL11
- S57 pad 2: Net-(D58-A) -> Net-(D56-A)
- S58 pad 1: /Key_Array/ICOL12 -> /Key_Array/ICOL11
- S58 pad 2: Net-(D59-A) -> Net-(D57-A)
- S59 pad 1: /Key_Array/ICOL12 -> /Key_Array/ICOL11
- S59 pad 2: Net-(D60-A) -> Net-(D58-A)
- S6 pad 2: Net-(D7-A) -> Net-(D5-A)
- S60 pad 1: /Key_Array/ICOL13 -> /Key_Array/ICOL11
- S60 pad 2: Net-(D61-A) -> Net-(D59-A)
- S61 pad 1: /Key_Array/ICOL13 -> /Key_Array/ICOL11
- S61 pad 2: Net-(D62-A) -> Net-(D60-A)
- S62 pad 1: /Key_Array/ICOL13 -> /Key_Array/ICOL12
- S62 pad 2: Net-(D63-A) -> Net-(D61-A)
- S63 pad 1: /Key_Array/ICOL13 -> /Key_Array/ICOL12
- S63 pad 2: Net-(D64-A) -> Net-(D62-A)
- S64 pad 1: /Key_Array/ICOL13 -> /Key_Array/ICOL12
- S64 pad 2: Net-(D65-A) -> Net-(D63-A)
- S65 pad 1: /Key_Array/ICOL14 -> /Key_Array/ICOL12
- S65 pad 2: Net-(D66-A) -> Net-(D64-A)
- S66 pad 1: /Key_Array/ICOL14 -> /Key_Array/ICOL12
- S66 pad 2: Net-(D67-A) -> Net-(D65-A)
- S67 pad 1: /Key_Array/ICOL14 -> /Key_Array/ICOL13
- S67 pad 2: Net-(D68-A) -> Net-(D66-A)
- S68 pad 1: /Key_Array/ICOL15 -> /Key_Array/ICOL13
- S68 pad 2: Net-(D69-A) -> Net-(D67-A)
- S7 pad 2: Net-(D8-A) -> Net-(D6-A)
- S8 pad 2: Net-(D9-A) -> Net-(D7-A)
- S9 pad 2: Net-(D10-A) -> Net-(D8-A)
- U3 pad 1: unconnected-(U3-NC-Pad1) -> +5V
- U3 pad 2: Net-(Q1-G) -> GND
- U3 pad 3: Net-(Q2-G) -> Net-(LED4-A)
- U3 pad 4: -BATT -> Net-(U3-STAT)
- U3 pad 5: Net-(U3-BAT) -> unconnected-(U3-SCL-Pad5)
- U3 pad 6: Net-(U3-V-) -> unconnected-(U3-SDA-Pad6)
- U4 pad 1: +5V -> unconnected-(U4-NC-Pad1)
- U4 pad 2: GND -> Net-(Q1-G)
- U4 pad 3: Net-(LED1-A) -> Net-(Q2-G)
- U4 pad 4: Net-(U4-STAT) -> -BATT
- U4 pad 5: unconnected-(U4-SCL-Pad5) -> Net-(U4-BAT)
- U4 pad 6: unconnected-(U4-SDA-Pad6) -> Net-(U4-V-)
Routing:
- net /Key_Array/IROW4: vias 0 -> 1
- net /Key_Array/IROW3: vias 0 -> 1
- net /Key_Array/IROW2: vias 0 -> 1
- net /Key_Array/IROW1: vias 0 -> 1
- net /Key_Array/IROW0: vias 0 -> 1
- net /Key_Array/ICOL9: vias 0 -> 1
- net /Key_Array/ICOL8: vias 0 -> 1
- net /Key_Array/ICOL7: vias 0 -> 1
- net /Key_Array/ICOL6: vias 0 -> 1
- net /Key_Array/ICOL5: vias 0 -> 1
- net /Key_Array/ICOL4: vias 0 -> 1
- net /Key_Array/ICOL3: vias 0 -> 1
- net /Key_Array/ICOL2: vias 0 -> 1
- net /Key_Array/ICOL13: vias 0 -> 1
- net /Key_Array/ICOL12: vias 0 -> 1
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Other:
- board size 81.3 x 50.8 mm -> 88.9 x 55.9 mm
- board text added: "+/=1"
- board text added: ":/;1"
- board text added: "</,1"
- board text added: ">/.1"
- board text added: "?//1"
- board text added: "A1"
- board text added: "B1"
- board text added: "BKSPC"
- board text added: "C1"
- board text added: "CAPS"
- board text added: "D1"
- board text added: "DEL"
- board text added: "DOWN1"
- board text added: "E1"
- board text added: "ENTER1"
- board text added: "ESC"
- board text added: "F1"
- board text added: "FN1"
- board text added: "FN2"
- board text added: "G1"
- board text added: "H1"
- board text added: "I1"
- board text added: "J1"
- board text added: "K1"
- board text added: "L1"
- board text added: "LCTRL"
- board text added: "LEFT1"
- board text added: "LSHIFT"
- board text added: "LSPCE1"
- board text added: "LSUP1"
- board text added: "M1"
- board text added: "N1"
- board text added: "NM0"
- board text added: "NM1"
- board text added: "NM2"
- board text added: "NM3"
- board text added: "NM4"
- board text added: "NM5"
- board text added: "NM6"
- board text added: "NM7"
- board text added: "NM8"
- board text added: "NM9"
- board text added: "O1"
- board text added: "P1"
- board text added: "PGDN1"
- board text added: "PGUP1"
- board text added: "R1"
- board text added: "RIGHT1"
- board text added: "RSPCE1"
- board text added: "RSUP1"
- board text added: "S1"
- board text added: "T1"
- board text added: "TAB1"
- board text added: "U1"
- board text added: "UP1"
- board text added: "V1"
- board text added: "W1"
- board text added: "X1"
- board text added: "Y1"
- board text added: "Z1"
- board text added: "\1"
- board text added: "_/-1"
- board text added: "{/[1"
- board text added: "{dblquote}/'1"
- board text added: "|/\1"
- board text added: "}/]1"
- board text removed: "1"
- board text removed: "Esc"

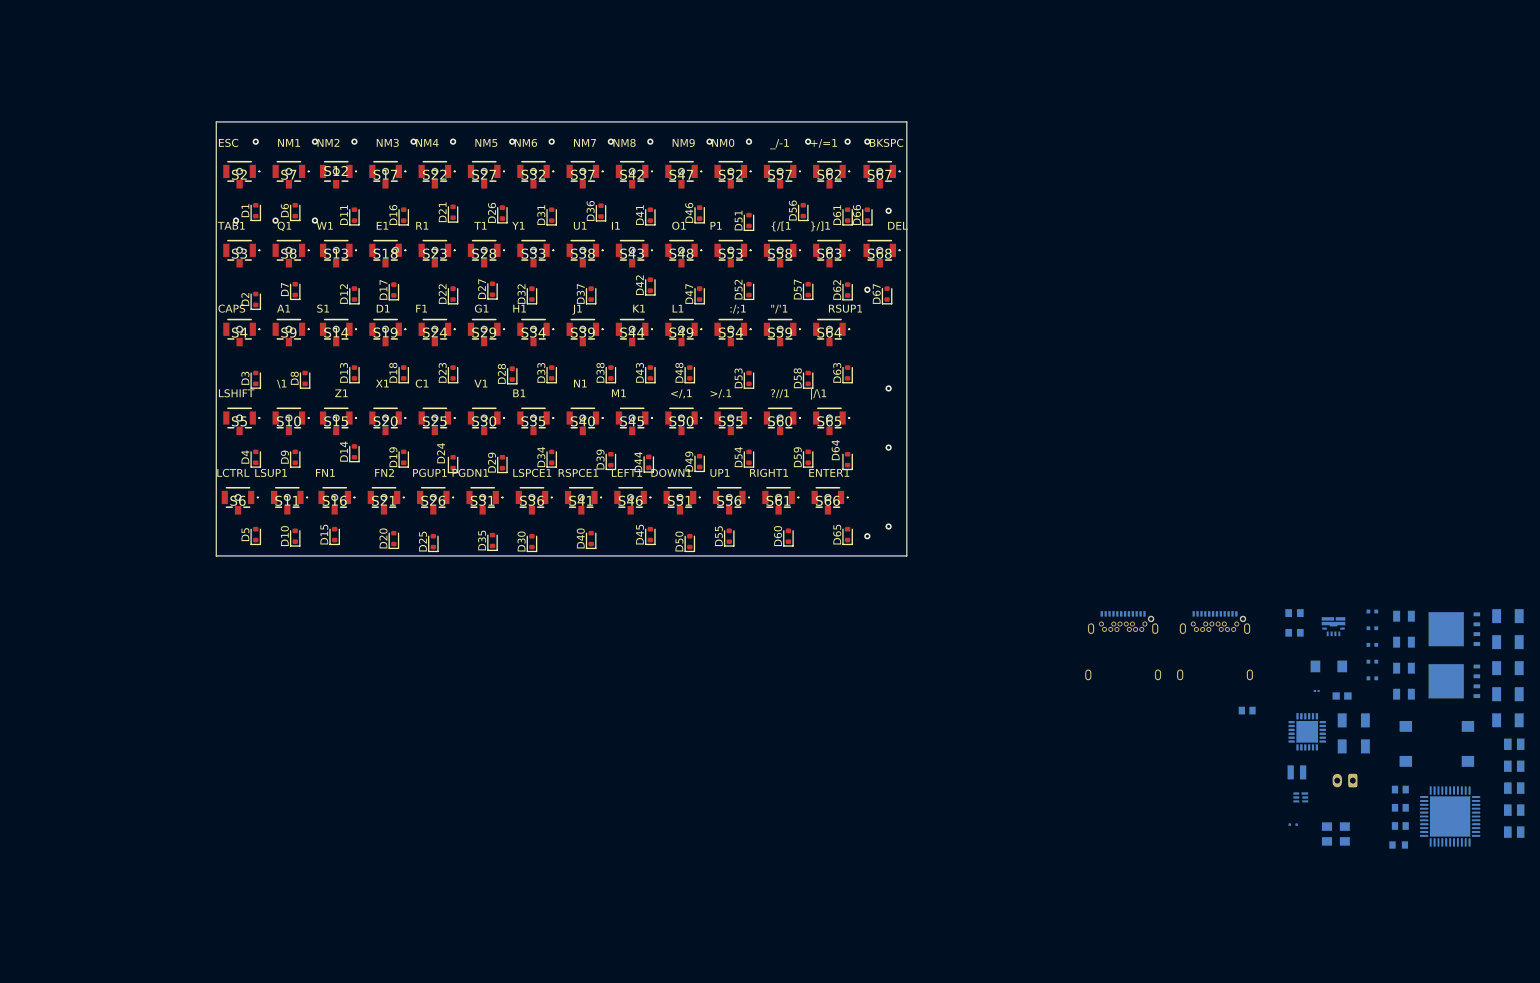
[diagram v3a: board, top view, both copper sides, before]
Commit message: Reorganised backside
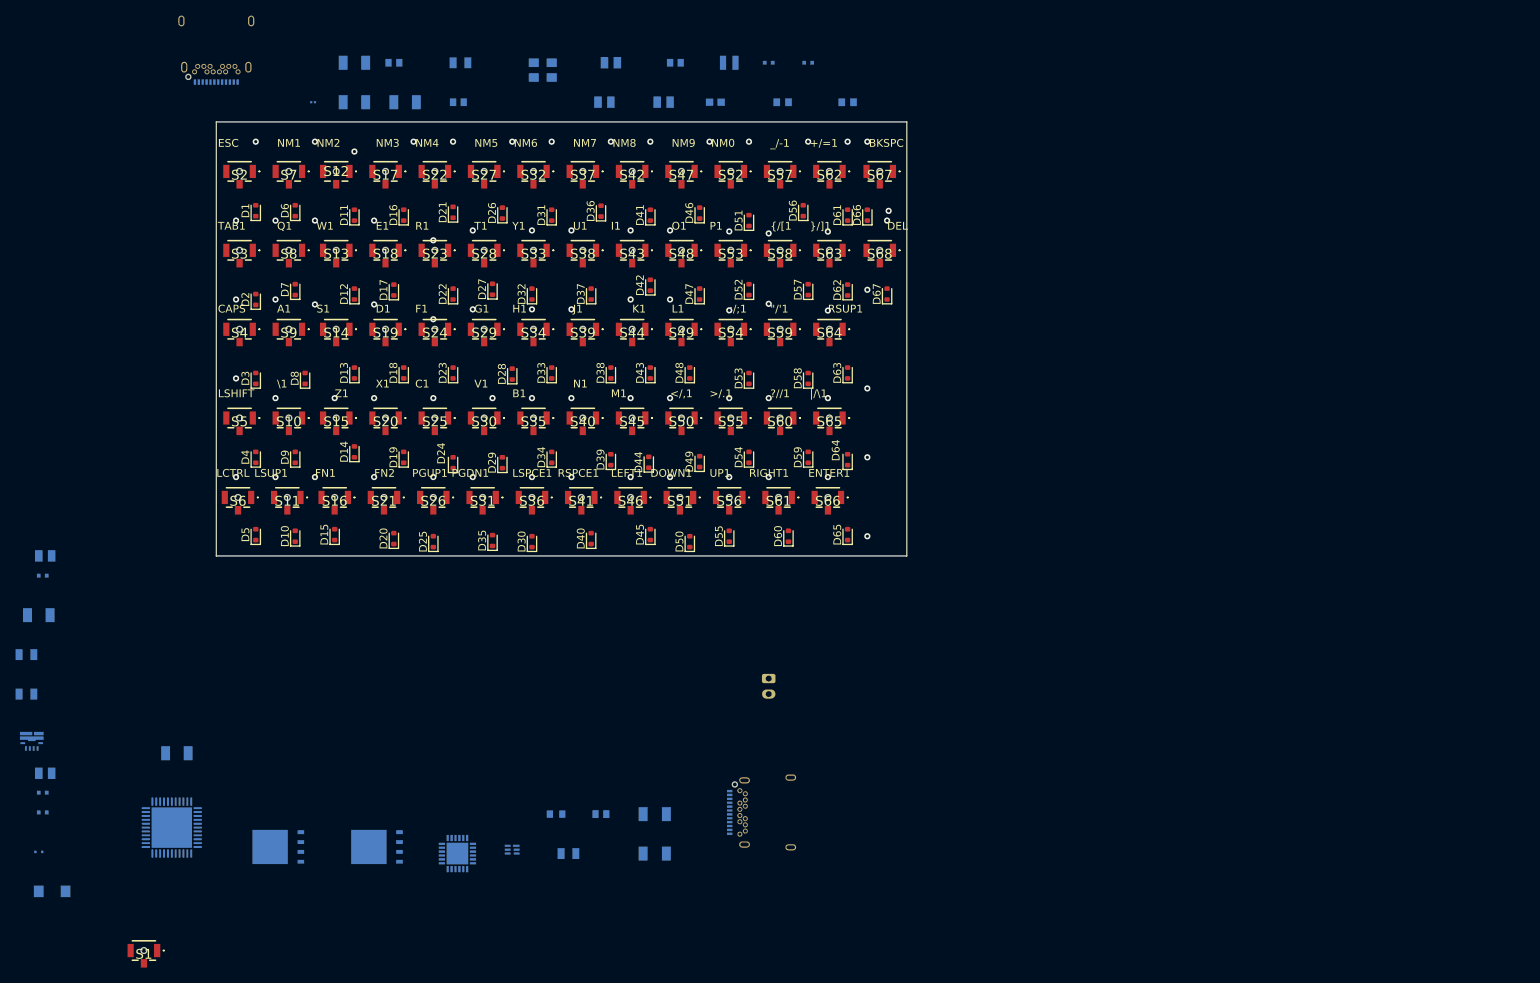
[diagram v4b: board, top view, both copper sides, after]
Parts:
- S1: value RESET -> B3U-1100P-B; footprint keyboard_syms:B3FS1012P -> keyboard_syms:B3U1100PB; moved to F.Cu
- moved C6 191.9 mm to (36.4, 91.4)
- moved R4 189.2 mm to (35.6, 99.1)
- moved C5 189.1 mm to (36.4, 119.4)
- moved LED3 177.4 mm to (34.0, 104.1)
- moved LED4 177.4 mm to (34.0, 109.2)
- moved R9 172.5 mm to (36.1, 124.5)
- moved R8 172.5 mm to (36.1, 121.9)
- moved R3 172.3 mm to (53.3, 116.8)
- moved R13 171.7 mm to (36.1, 94.0)
- moved S1 168.6 mm to (49.1, 142.2), turned to 0 degrees
- moved U2 168.2 mm to (35.6, 114.3)
- moved R5 167.7 mm to (76.2, 27.9)
- moved R14 166.9 mm to (76.2, 33.0)
- moved R16 166.9 mm to (37.3, 134.6)
- moved U1 164.6 mm to (52.7, 126.4)
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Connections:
- R3 pad 2: Net-(S1-N2) -> Net-(S1-C1)
- S1 pad 1: GND -> Net-(S1-C1)
- S1 pad 2: unconnected-(S1-C2-Pad2) -> GND
- U1 pad 13: Net-(S1-N2) -> Net-(S1-C1)
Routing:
- net Net-(U3-TS1): vias 0 -> 2
- net Net-(U1-XTAL2): vias 0 -> 1
- net Net-(LED4-A): vias 0 -> 1
- net Net-(LED1-A): vias 0 -> 1
- net GND: vias 0 -> 2
- net /Key_Array/ICOL9: vias 1 -> 5
- net /Key_Array/ICOL8: vias 1 -> 5
- net /Key_Array/ICOL7: vias 1 -> 4
- net /Key_Array/ICOL6: vias 1 -> 5
- net /Key_Array/ICOL5: vias 1 -> 4
- net /Key_Array/ICOL4: vias 1 -> 5
- net /Key_Array/ICOL3: vias 1 -> 5
- net /Key_Array/ICOL2: vias 1 -> 3
- net /Key_Array/ICOL13: vias 1 -> 2
- net /Key_Array/ICOL12: vias 1 -> 4
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
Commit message: "Finished" board layout
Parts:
- L1, LED3, R10, R12, R9, U2: moved to F.Cu
- moved R16 125.3 mm to (130.4, 50.8)
- moved S1 118.1 mm to (78.7, 27.9)
- moved Q2 111.9 mm to (129.3, 36.4)
- moved L1 106.8 mm to (86.4, 35.6), turned to -90 degrees
- moved R8 104.6 mm to (86.9, 30.5)
- moved U3 103.8 mm to (119.9, 30.5)
- moved LED4 102.8 mm to (105.7, 35.6)
- moved Q1 99.8 mm to (129.2, 42.5)
- moved LED3 99.4 mm to (100.7, 30.5), turned to 0 degrees
- moved U4 99.0 mm to (141.7, 41.1)
- moved R13 98.7 mm to (118.0, 39.0)
- moved U2 98.1 mm to (94.9, 36.2), turned to 0 degrees
- moved C5 97.9 mm to (74.0, 29.0)
- moved R9 96.0 mm to (94.5, 48.3), turned to 0 degrees
- moved P2 95.4 mm to (141.9, 29.9)
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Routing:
- net GND: track 0.00 -> 359.6 mm, vias 2 -> 5
- net /Key_Array/IROW3: track 0.00 -> 203.7 mm
- net /Key_Array/IROW0: track 0.00 -> 152.5 mm, vias 1 -> 6
- net /Key_Array/IROW4: track 0.00 -> 152.5 mm
- net /Key_Array/IROW2: track 0.00 -> 151.9 mm, vias 1 -> 4
- net /Key_Array/IROW1: track 0.00 -> 147.0 mm, vias 1 -> 7
- net /Key_Array/ICOL12: track 0.00 -> 146.7 mm, vias 4 -> 1
- net /Key_Array/ICOL11: track 0.00 -> 144.2 mm, vias 5 -> 3
- net /Key_Array/ICOL9: track 0.00 -> 143.7 mm, vias 5 -> 3
- net /Key_Array/ICOL4: track 0.00 -> 138.4 mm, vias 5 -> 2
- net /MCU_Battery/VBUSOUT: track 0.00 -> 137.1 mm, vias 0 -> 6
- net /Key_Array/ICOL7: track 0.00 -> 120.4 mm, vias 4 -> 1
- net /Key_Array/ICOL10: track 0.00 -> 114.9 mm, vias 4 -> 3
- net /Key_Array/ICOL8: track 0.00 -> 110.1 mm
- net +BATT: track 0.00 -> 104.7 mm, vias 0 -> 4
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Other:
- board size 88.9 x 55.9 mm -> 88.9 x 86.4 mm
